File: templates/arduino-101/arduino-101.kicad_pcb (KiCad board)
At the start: 2 copper layers, 68.6 x 53.3 mm, 5 parts, among them U1 HOLE, U2 HOLE, U3 HOLE, U4 HOLE, U5 ARDUINO-101-SHIELD

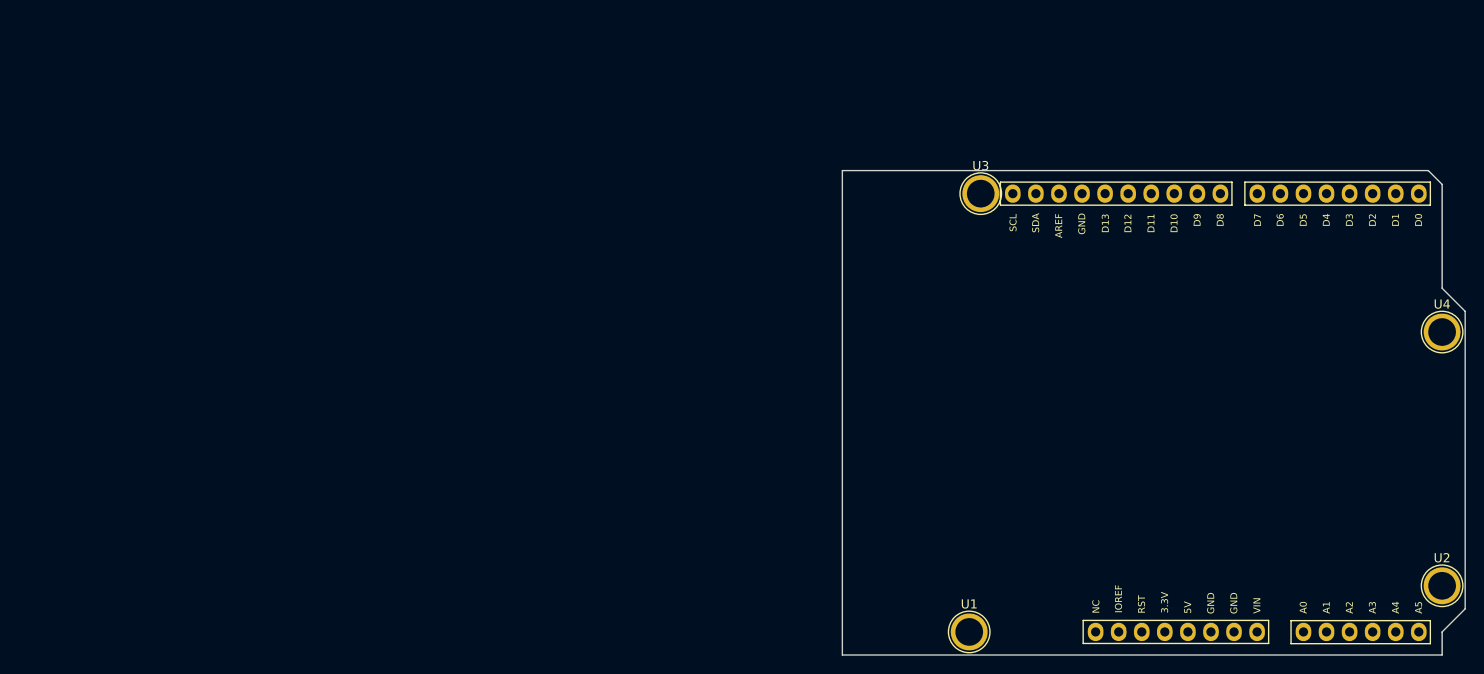
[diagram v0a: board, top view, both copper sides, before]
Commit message: Add fab notes to Dwgs.User
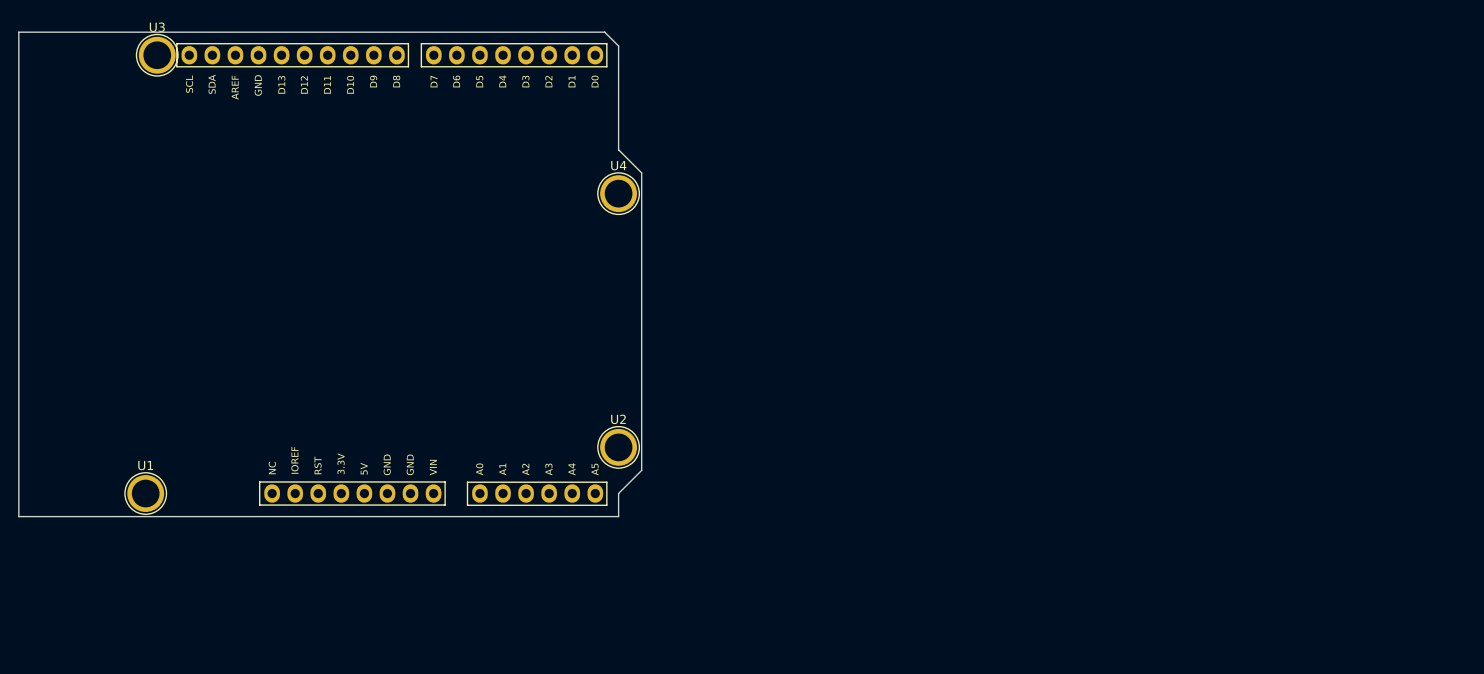
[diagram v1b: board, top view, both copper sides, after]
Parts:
- moved U2 91.9 mm to (86.4, 103.5)
- moved U4 91.9 mm to (86.4, 75.6)
- moved U1 91.9 mm to (34.3, 108.6)
- moved U3 91.9 mm to (35.6, 60.3)
- moved U5 91.9 mm to (43.1, 108.6)
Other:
- board text added: "FABRICATION NOTES 1. THIS IS A 2 LAYER BOARD. 2. EXTERNAL LAYERS SHALL HAVE 1 OZ COPPER. 3. MATERIAL: FR4 AND 0.062 INCH +/- 10% THICK. 4. BOARDS SHALL BE ROHS COMPLIANT. 5. MANUFACTURE IN ACCORDANCE WITH IPC-6012 CLASS 2 6. MASK: BOTH SIDES OF THE BOARD SHALL HAVE SOLDER MASK (ANY COLOR) OVER BARE COPPER. 7. SILK: BOTH SIDES OF THE BOARD SHALL HAVE WHITE SILKSCREEN. DO NOT PLACE SILK OVER BARE C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"
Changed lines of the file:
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@@
-(kicad_pcb (version 4) (host pcbnew 4.0.5-e0-6337~49~ubuntu16.04.1)
+(kicad_pcb (version 4) (host pcbnew 4.0.7-e2-6376~58~ubuntu16.04.1)
   (general
     (links 4)
@@
     (area 110.922999 71.488 179.653001 129.272)
     (thickness 1.6)
-    (drawings 9)
+    (drawings 10)
     (tracks 0)
     (zones 0)
@@
   )
   (module Wickerlib:ARDUINO-101-SHIELD locked (layer F.Cu)
-    (at 133.8072 123.825)
+    (at 43.1292 108.585)
     (descr "Through hole socket strip")
     (tags "socket strip")
@@
   )
   (module ARDUINO-MOUNTING-HOLE locked (layer F.Cu)
-    (at 124.968 123.825)
+    (at 34.29 108.585)
     (descr "module 1 pin (ou trou mecanique de percage)")
     (tags DEV)
@@
   )
   (module ARDUINO-MOUNTING-HOLE locked (layer F.Cu)
-    (at 177.038 118.745)
+    (at 86.36 103.505)
     (descr "module 1 pin (ou trou mecanique de percage)")
     (tags DEV)
@@
   )
   (module ARDUINO-MOUNTING-HOLE locked (layer F.Cu)
-    (at 126.238 75.565)
+    (at 35.56 60.325)
     (descr "module 1 pin (ou trou mecanique de percage)")
     (tags DEV)
@@
   )
   (module ARDUINO-MOUNTING-HOLE locked (layer F.Cu)
-    (at 177.038 90.805)
+    (at 86.36 75.565)
     (descr "module 1 pin (ou trou mecanique de percage)")
     (tags DEV)
@@
     (pad 1 thru_hole circle (at 0 0) (size 4.064 4.064) (drill 3.048) (layers *.Cu *.Mask F.SilkS))
   )
-  (gr_line (start 177.038 74.549) (end 175.514 73.025) (angle 90) (layer Edge.Cuts) (width 0.15))
-  (gr_line (start 177.038 85.979) (end 177.038 74.549) (angle 90) (layer Edge.Cuts) (width 0.15))
-  (gr_line (start 179.578 88.519) (end 177.038 85.979) (angle 90) (layer Edge.Cuts) (width 0.15))
-  (gr_line (start 179.578 121.285) (end 179.578 88.519) (angle 90) (layer Edge.Cuts) (width 0.15))
-  (gr_line (start 177.038 123.825) (end 179.578 121.285) (angle 90) (layer Edge.Cuts) (width 0.15))
-  (gr_line (start 177.038 126.365) (end 177.038 123.825) (angle 90) (layer Edge.Cuts) (width 0.15))
-  (gr_line (start 110.998 126.365) (end 177.038 126.365) (angle 90) (layer Edge.Cuts) (width 0.15))
-  (gr_line (start 110.998 73.025) (end 110.998 126.365) (angle 90) (layer Edge.Cuts) (width 0.15))
-  (gr_line (start 175.514 73.025) (end 110.998 73.025) (angle 90) (layer Edge.Cuts) (width 0.15))
+  (gr_text "FABRICATION NOTES\n\n1. THIS IS A 2 LAYER BOARD. \n2. EXTERNAL LAYERS SHALL HAVE 1 OZ COPPER.\n3. MATERIAL: FR4 AND 0.062 INCH +/- 10% THICK.\n4. BOARDS SHALL BE ROHS COMPLIANT. \n5. MANUFACTURE IN ACCORDANCE WITH IPC-6012 CLASS 2\n6. MASK: BOTH SIDES OF THE BOARD SHALL HAVE \n   SOLDER MASK (ANY COLOR) OVER BARE COPPER. \n7. SILK: BOTH SIDES OF THE BOARD SHALL HAVE \n   WHITE SILKSCREEN. DO NOT PLACE SILK OVER BARE COPPER.\n8. FINISH: ENIG.\n9. MINIMUM TRACE WIDTH - 0.006 INCH.\n   MINIMUM SPACE - 0.006 INCH.\n   MINIMUM HOLE DIA - 0.013 INCH. \n10. MAX HOLE PLACEMENT TOLERANCE OF +/- 0.003 INCH.\n11. MAX HOLE DIAMETER TOLERANCE OF +/- 0.003 INCH AFTER PLATING." (at 103.2256 90.1192) (layer Dwgs.User)
+    (effects (font (size 2.54 2.54) (thickness 0.254)) (justify left))
+  )
+  (gr_line (start 86.36 59.309) (end 84.836 57.785) (angle 90) (layer Edge.Cuts) (width 0.15))
+  (gr_line (start 86.36 70.739) (end 86.36 59.309) (angle 90) (layer Edge.Cuts) (width 0.15))
+  (gr_line (start 88.9 73.279) (end 86.36 70.739) (angle 90) (layer Edge.Cuts) (width 0.15))
+  (gr_line (start 88.9 106.045) (end 88.9 73.279) (angle 90) (layer Edge.Cuts) (width 0.15))
+  (gr_line (start 86.36 108.585) (end 88.9 106.045) (angle 90) (layer Edge.Cuts) (width 0.15))
+  (gr_line (start 86.36 111.125) (end 86.36 108.585) (angle 90) (layer Edge.Cuts) (width 0.15))
+  (gr_line (start 20.32 111.125) (end 86.36 111.125) (angle 90) (layer Edge.Cuts) (width 0.15))
+  (gr_line (start 20.32 57.785) (end 20.32 111.125) (angle 90) (layer Edge.Cuts) (width 0.15))
+  (gr_line (start 84.836 57.785) (end 20.32 57.785) (angle 90) (layer Edge.Cuts) (width 0.15))
 )
